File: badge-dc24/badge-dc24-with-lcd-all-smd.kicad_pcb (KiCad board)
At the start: 2 copper layers, 31 parts, among them P1 USB_OTG, U1 ESP-12E, U2 TSOP38238, U3 74HC595, U4 MC78L05ACH

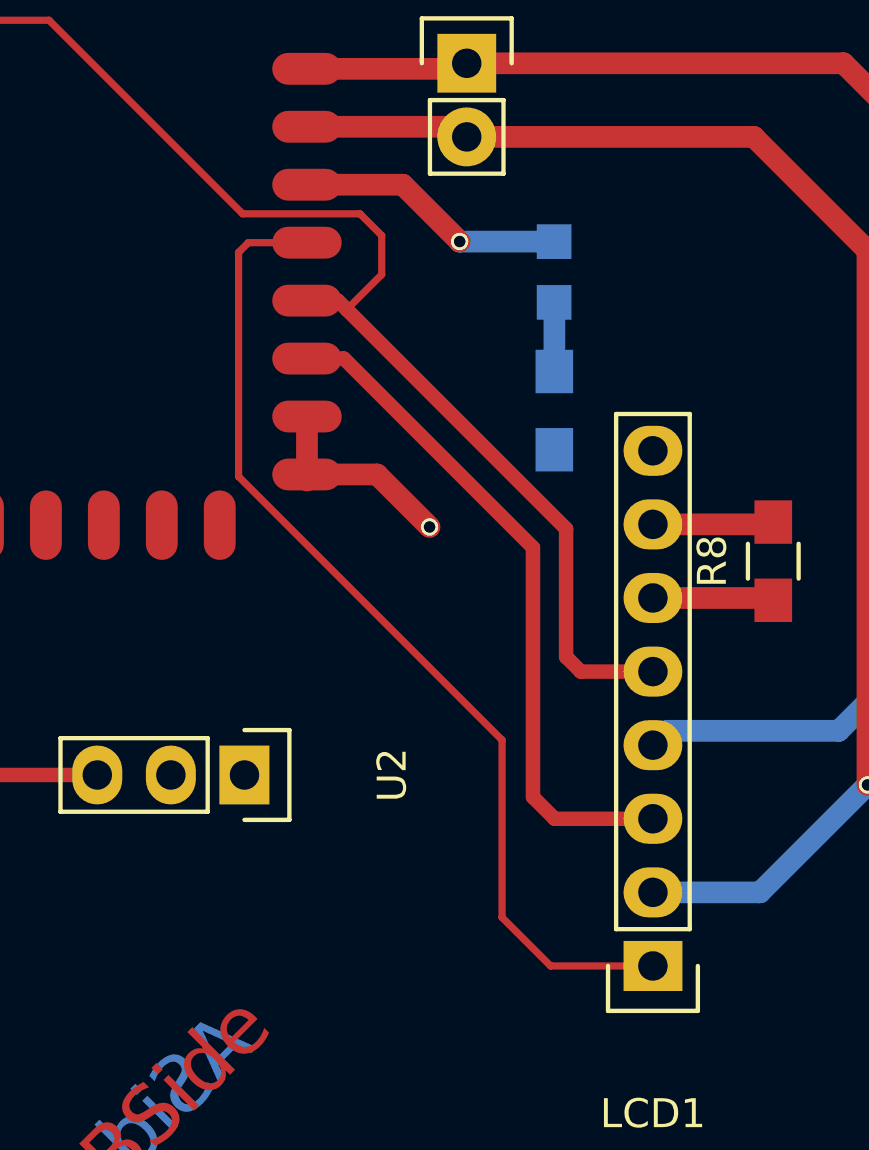
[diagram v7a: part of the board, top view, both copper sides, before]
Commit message: Moved IR LED into a central position
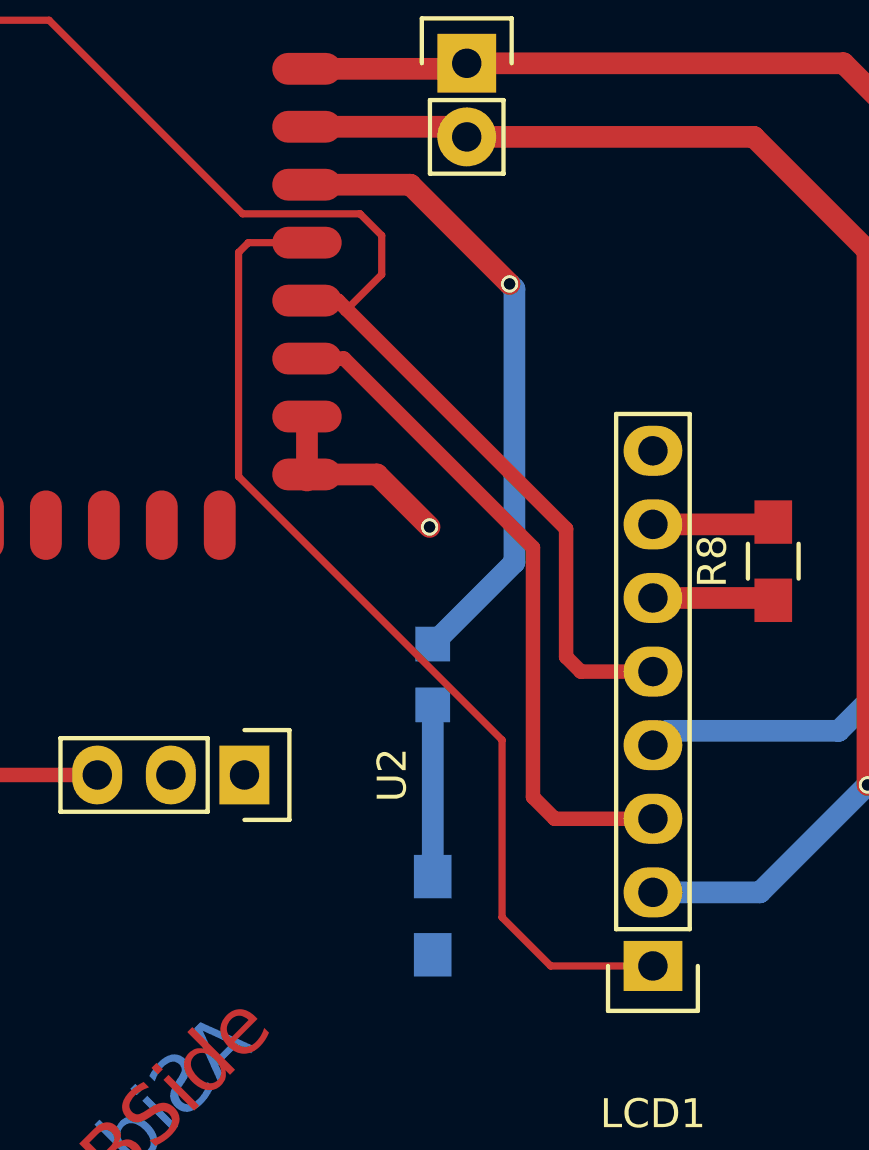
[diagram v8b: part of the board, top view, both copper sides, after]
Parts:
- moved R2 17.9 mm to (96.1, 101.5)
- moved Infrared1 14.5 mm to (96.1, 93.2)
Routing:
- net Net-(Infrared1-Pad2): track 9.34 -> 22.1 mm
- net Net-(Infrared1-Pad1): track 2.39 -> 5.94 mm
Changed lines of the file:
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@@
     (links 74)
     (no_connects 0)
-    (area 0 0 0 0)
+    (area 49.57 58.46 152.36 130.77)
     (thickness 1.6)
     (drawings 13)
-    (tracks 206)
+    (tracks 207)
     (zones 0)
     (modules 31)
@@
   )
   (module Resistors_SMD:R_0805_HandSoldering (layer B.Cu)
-    (at 100.2538 84.0486 90)
+    (at 96.05772 101.47808 90)
     (descr "Resistor SMD 0805, hand soldering")
     (tags "resistor 0805")
@@
   )
   (module LEDs:LED_0805 (layer B.Cu)
-    (at 100.24872 79.26324 90)
+    (at 96.05772 93.15196 90)
     (descr "LED 0805 smd package")
     (tags "LED 0805 SMD")
@@
   (segment (start 56.769 82.4484) (end 61.5696 82.4484) (width 0.75) (layer F.Cu) (net 13))
   (segment (start 61.5696 82.4484) (end 61.7474 82.2706) (width 0.75) (layer F.Cu) (net 13))
-  (segment (start 131.1656 66.9544) (end 131.1656 65.99428) (width 0.25) (layer F.Cu) (net 15) (status C00000))
-  (segment (start 131.1656 65.99428) (end 132.19176 64.96812) (width 0.25) (layer F.Cu) (net 15) (status 400000))
-  (segment (start 140.45322 67.79652) (end 142.4961 67.79652) (width 0.25) (layer F.Cu) (net 15) (status 800000))
+  (segment (start 131.1656 66.9544) (end 131.1656 65.99428) (width 0.25) (layer F.Cu) (net 15))
+  (segment (start 131.1656 65.99428) (end 132.19176 64.96812) (width 0.25) (layer F.Cu) (net 15))
+  (segment (start 140.45322 67.79652) (end 142.4961 67.79652) (width 0.25) (layer F.Cu) (net 15))
   (segment (start 137.62482 64.96812) (end 140.45322 67.79652) (width 0.25) (layer F.Cu) (net 15))
   (segment (start 132.19176 64.96812) (end 137.62482 64.96812) (width 0.25) (layer F.Cu) (net 15))
@@
   (segment (start 91.7174 84.2503) (end 91.7174 86.2503) (width 0.75) (layer F.Cu) (net 15) (status 30))
   (segment (start 91.7174 86.2503) (end 91.7174 86.4596) (width 0.75) (layer F.Cu) (net 15) (status 30))
-  (segment (start 91.7174 76.2503) (end 95.02598 76.2503) (width 0.75) (layer F.Cu) (net 16))
-  (segment (start 96.9899 78.21422) (end 100.24872 78.21422) (width 0.75) (layer B.Cu) (net 16))
-  (segment (start 96.98736 78.21168) (end 96.9899 78.21422) (width 0.75) (layer B.Cu) (net 16))
-  (via (at 96.98736 78.21168) (size 0.6) (drill 0.4) (layers F.Cu B.Cu) (net 16))
-  (segment (start 95.02598 76.2503) (end 96.98736 78.21168) (width 0.75) (layer F.Cu) (net 16))
+  (segment (start 91.7174 76.2503) (end 95.28506 76.2503) (width 0.75) (layer F.Cu) (net 16) (status 400000))
+  (segment (start 98.87712 89.28354) (end 96.05772 92.10294) (width 0.75) (layer B.Cu) (net 16) (status 800000))
+  (segment (start 98.87712 79.84236) (end 98.87712 89.28354) (width 0.75) (layer B.Cu) (net 16))
+  (segment (start 98.70948 79.67472) (end 98.87712 79.84236) (width 0.75) (layer B.Cu) (net 16))
+  (via (at 98.70948 79.67472) (size 0.6) (drill 0.4) (layers F.Cu B.Cu) (net 16))
+  (segment (start 95.28506 76.2503) (end 98.70948 79.67472) (width 0.75) (layer F.Cu) (net 16))
   (segment (start 66.30416 108.43134) (end 66.30416 105.44556) (width 0.75) (layer B.Cu) (net 17) (status 30))
   (segment (start 69.17436 108.36784) (end 69.17436 105.35666) (width 0.75) (layer B.Cu) (net 18) (status 30))
@@
   (segment (start 73.74128 93.79712) (end 73.74128 84.91728) (width 0.5) (layer F.Cu) (net 31))
   (segment (start 76.56576 96.6216) (end 73.74128 93.79712) (width 0.5) (layer F.Cu) (net 31))
-  (segment (start 100.2538 82.6986) (end 100.2538 80.31734) (width 0.75) (layer B.Cu) (net 32))
-  (segment (start 100.2538 80.31734) (end 100.24872 80.31226) (width 0.75) (layer B.Cu) (net 32))
+  (segment (start 96.05772 100.12808) (end 96.05772 94.20098) (width 0.75) (layer B.Cu) (net 32) (status C00000))
+  (segment (start 96.06534 100.12046) (end 96.05772 100.12808) (width 0.75) (layer B.Cu) (net 32))
   (segment (start 91.7174 82.2503) (end 92.9945 82.2503) (width 0.5) (layer F.Cu) (net 33) (status 10))
   (segment (start 100.2665 98.1329) (end 103.6574 98.1329) (width 0.5) (layer F.Cu) (net 33) (status 20))
@@
   (segment (start 67.02044 80.66024) (end 67.02044 81.65084) (width 0.5) (layer F.Cu) (net 40))
   (segment (start 63.6486 77.2884) (end 67.02044 80.66024) (width 0.5) (layer F.Cu) (net 40))
-  (segment (start 133.6602 71.8693) (end 138.7094 71.8693) (width 0.25) (layer F.Cu) (net 41) (status 400000))
-  (segment (start 140.18218 70.39652) (end 142.4961 70.39652) (width 0.25) (layer F.Cu) (net 41) (status 800000))
+  (segment (start 133.6602 71.8693) (end 138.7094 71.8693) (width 0.25) (layer F.Cu) (net 41))
+  (segment (start 140.18218 70.39652) (end 142.4961 70.39652) (width 0.25) (layer F.Cu) (net 41))
   (segment (start 138.7094 71.8693) (end 140.18218 70.39652) (width 0.25) (layer F.Cu) (net 41))
   (segment (start 120.17756 69.80174) (end 120.17756 72.19696) (width 0.75) (layer F.Cu) (net 41) (status 10))
@@
   (segment (start 133.6602 71.8693) (end 133.6602 66.9998) (width 0.75) (layer F.Cu) (net 41) (status 30))
   (segment (start 133.6602 66.9998) (end 133.7056 66.9544) (width 0.75) (layer F.Cu) (net 41) (status 30))
-  (segment (start 145.1961 65.59652) (end 145.1961 72.59652) (width 0.75) (layer F.Cu) (net 45) (status C00000))
-  (segment (start 142.4961 71.59652) (end 144.1961 71.59652) (width 0.75) (layer F.Cu) (net 45) (status 400000))
-  (segment (start 144.1961 71.59652) (end 145.1961 72.59652) (width 0.75) (layer F.Cu) (net 45) (status 800000))
-  (segment (start 142.4961 66.59652) (end 144.1961 66.59652) (width 0.75) (layer F.Cu) (net 45) (status 400000))
-  (segment (start 144.1961 66.59652) (end 145.1961 65.59652) (width 0.75) (layer F.Cu) (net 45) (status 800000))
+  (segment (start 145.1961 65.59652) (end 145.1961 72.59652) (width 0.75) (layer F.Cu) (net 45))
+  (segment (start 142.4961 71.59652) (end 144.1961 71.59652) (width 0.75) (layer F.Cu) (net 45))
+  (segment (start 144.1961 71.59652) (end 145.1961 72.59652) (width 0.75) (layer F.Cu) (net 45))
+  (segment (start 142.4961 66.59652) (end 144.1961 66.59652) (width 0.75) (layer F.Cu) (net 45))
+  (segment (start 144.1961 66.59652) (end 145.1961 65.59652) (width 0.75) (layer F.Cu) (net 45))
   (zone (net 1) (net_name +3V3) (layer F.Cu) (hatch edge 0.508)
     (connect_pads (clearance 0.508))
